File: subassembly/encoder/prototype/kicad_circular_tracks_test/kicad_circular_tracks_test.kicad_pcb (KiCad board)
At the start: 4 copper layers, 39 x 39 mm, 35 parts, among them J1 Conn_01x05, J2 Conn_01x05, U1 ATSAMD10D13A-M

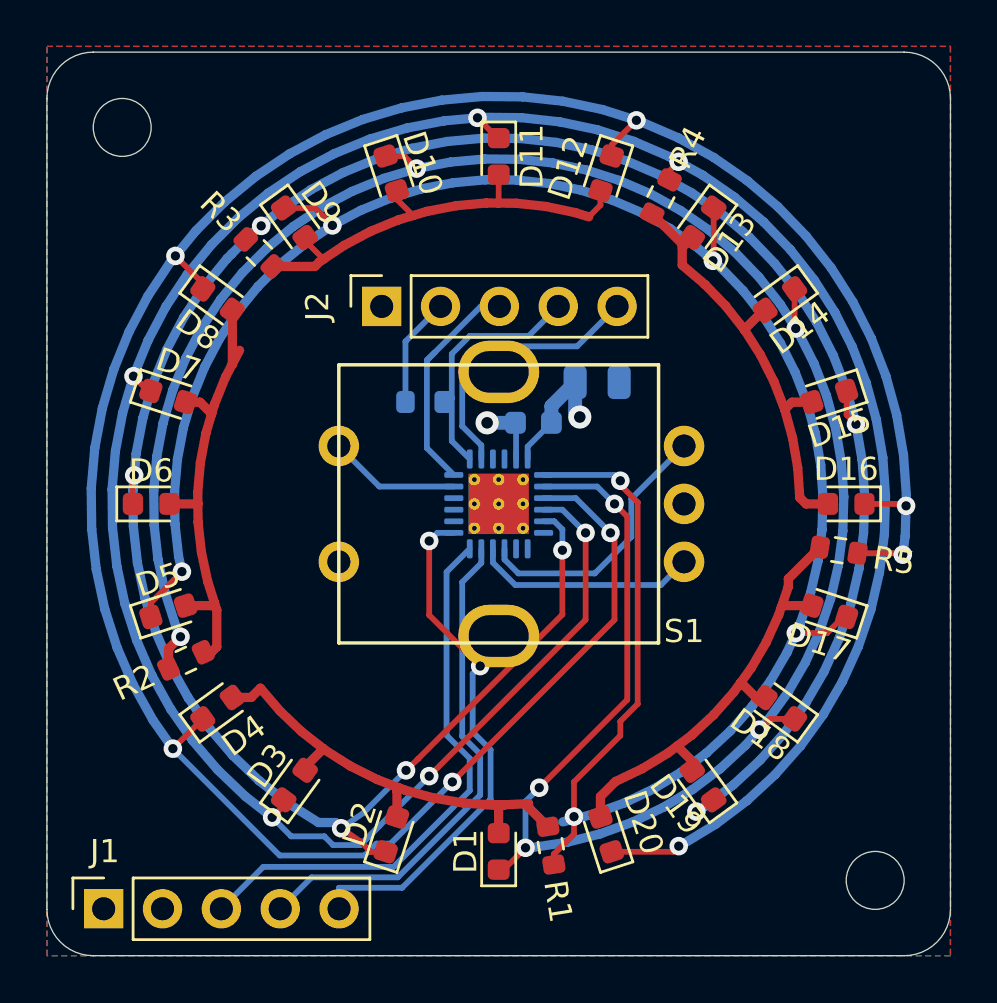
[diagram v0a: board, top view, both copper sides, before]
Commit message: SOICbite connector, RC filters for inputs
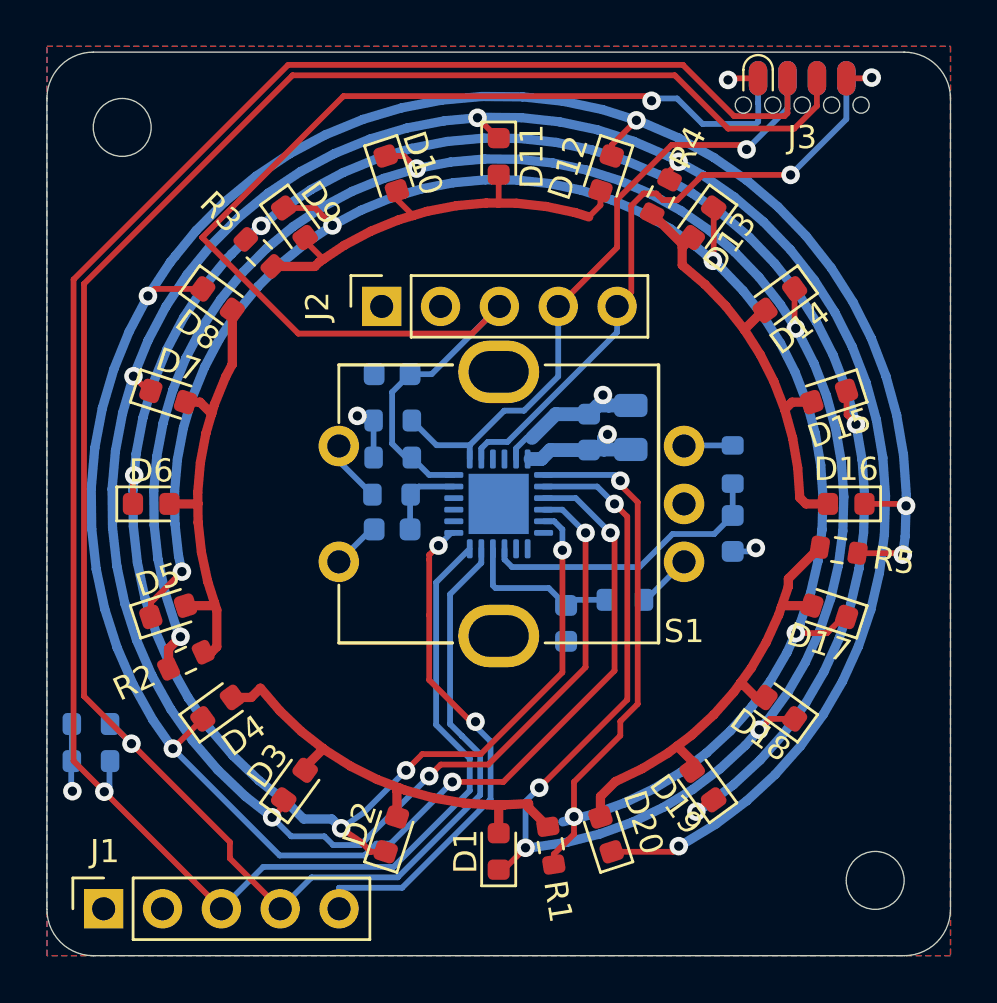
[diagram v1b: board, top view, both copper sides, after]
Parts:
- added C3: 0.1uF, Capacitor_SMD:C_0603_1608Metric, B.Cu at (152.9, 105.2)
- added C4: 0.1uF, Capacitor_SMD:C_0603_1608Metric, B.Cu at (160.1, 101.3)
- added C5: 0.1uF, Capacitor_SMD:C_0603_1608Metric, B.Cu at (145.4, 101.1)
- added C6: 0.1uF, Capacitor_SMD:C_0603_1608Metric, B.Cu at (145.4, 94.4)
- added J3: SOICbite-SWD, BVH_SOICbite:SOICbite_renumbered, F.Cu at (163.1, 80.5)
- added R10: 1k, Resistor_SMD:R_0603_1608Metric, B.Cu at (160.1, 98.3)
- added R11: 1k, Resistor_SMD:R_0603_1608Metric, B.Cu at (145.4, 99.6)
- added R12: 10k, Resistor_SMD:R_0603_1608Metric, B.Cu at (145.4, 98.0)
- added R7: 2k2, Resistor_SMD:R_0603_1608Metric, B.Cu at (132.4, 111.1)
- added R8: 2k2, Resistor_SMD:R_0603_1608Metric, B.Cu at (132.4, 109.5)
- added R9: 1k, Resistor_SMD:R_0603_1608Metric, B.Cu at (155.4, 104.1)
- U1: footprint Package_DFN_QFN:QFN-24-1EP_4x4mm_P0.5mm_EP2.6x2.6mm_ThermalVias -> Package_DFN_QFN:QFN-24-1EP_4x4mm_P0.5mm_EP2.6x2.6mm
- moved C1 2.43 mm to (153.9, 96.9), turned to 90 degrees
- moved C2 2.43 mm to (155.7, 96.7), turned to 90 degrees
- moved R6 1.59 mm to (145.4, 96.4)
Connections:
- net +3V3 renamed +3.3V
- net ~RESET renamed ~{RESET}
- S1 pad 1: ENC_SW -> ENC_SW_RAW
- S1 pad 3: ENC_A -> ENC_A_RAW
- S1 pad 5: ENC_B -> ENC_B_RAW
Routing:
- net I2C_SDA: track 22.0 -> 92.1 mm, vias 0 -> 1
- net I2C_SCL: track 24.1 -> 92.8 mm, vias 0 -> 1
- net ~{RESET}: track 10.0 -> 55.7 mm, vias 0 -> 1
- net SWCLK: track 10.7 -> 27.7 mm, vias 0 -> 1
- net SWDIO: track 12.2 -> 26.9 mm, vias 0 -> 1
- net GND: track 2.82 -> 11.0 mm, vias 1 -> 3
- net ENC_A: track 9.66 -> 6.91 mm
- net ENC_SW_RAW: track 0.00 -> 2.70 mm
- net ENC_A_RAW: track 0.00 -> 2.41 mm
- net ENC_SW: track 5.69 -> 3.52 mm
- net ENC_B_RAW: track 0.00 -> 2.11 mm
- net E: track 110.8 -> 112.7 mm
- net C: track 107.9 -> 109.5 mm
- net +3.3V: track 10.5 -> 11.8 mm, vias 1 -> 4
- net ENC_B: track 11.7 -> 12.7 mm
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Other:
- board text added: "I2C Term"
- board text added: "~{RST}"
- board text removed: "~RST"

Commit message: WIP
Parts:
- removed G***: LOGO, BVH_Logos:SkyIron_logo_Back
- removed J2: Conn_01x05, Connector_PinSocket_2.54mm:PinSocket_1x05_P2.54mm_Vertical
- added J4: Conn_01x05, Connector_PinSocket_1.27mm:PinSocket_1x05_P1.27mm_Vertical, B.Cu at (133.0, 112.5)
- added R13: ?, Resistor_SMD:R_0603_1608Metric, B.Cu at (157.8, 94.5)
- added R14: ?, Resistor_SMD:R_0603_1608Metric, B.Cu at (159.2, 94.5)
- J1: footprint Connector_PinSocket_2.54mm:PinSocket_1x05_P2.54mm_Vertical -> Connector_PinSocket_1.27mm:PinSocket_1x05_P1.27mm_Vertical; moved to B.Cu
- moved J3 34.0 mm to (130.5, 90.0), turned to -90 degrees
- moved J1 33.9 mm to (166.5, 112.5), turned to 0 degrees
- moved R7 7.34 mm to (136.0, 117.5)
- moved R8 7.34 mm to (136.0, 115.9)
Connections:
- U1 pad 1: A -> ADDR_SET
- U1 pad 2: B -> A
- U1 pad 3: E -> B
- U1 pad 4: D -> E
- U1 pad 5: C -> D
- U1 pad 6: unconnected-(U1-Pad6) -> C
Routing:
- net +3.3V: track 11.8 -> 109.5 mm, vias 4 -> 3
- net INT: track 22.2 -> 54.3 mm, vias 2 -> 3
- net ~{RESET}: track 55.7 -> 24.7 mm, vias 1 -> 2
- net I2C_SCL: track 92.8 -> 80.7 mm, vias 1 -> 2
- net I2C_SDA: track 92.1 -> 81.2 mm, vias 1 -> 2
- net ADDR_SET: track 0.00 -> 9.86 mm
- net SWDIO: track 26.9 -> 23.7 mm, vias 1 -> 2
- net SWCLK: track 27.7 -> 25.0 mm, vias 1 -> 2
- net GND: track 11.0 -> 12.2 mm, vias 3 -> 14
- net C: track 109.5 -> 108.8 mm
- net D: track 118.6 -> 118.0 mm
- added copper zone on In2.Cu, net GND
- removed copper zone on In2.Cu, net +3.3V
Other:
- board text removed: "3.3V"
- board text removed: "CLK"
- board text removed: "DAT"
- board text removed: "GND"
- board text removed: "INT"
- board text removed: "SCL"
- board text removed: "SDA"
- board text removed: "~{RST}"

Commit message: Keyboard matrix prototype + encoder update
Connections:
- U1 pad 25: (no net) -> GND
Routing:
- net GND: track 12.2 -> 14.5 mm, vias 14 -> 20
